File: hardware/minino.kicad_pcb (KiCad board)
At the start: 2 copper layers, 45 x 68 mm, 55 parts, among them J1 OLED, J2 GPS, J3 Battery, P1 USB_C_Plug_USB2.0, Q1 DMG3415U-7, Q2 PN2222A, SW1 ON, SW2 RIGHT, SW3 LEFT, SW4 DOWN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

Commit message: Replace_Labels
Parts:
- moved kibuzzard-6397A6E0 96.6 mm to (195.1, 91.4)
- moved kibuzzard-6398BE6D 92.2 mm to (200.9, 42.7), turned to 180 degrees
- moved kibuzzard-6397A7CD 89.3 mm to (186.8, 82.9)
- moved kibuzzard-6397A7DE 88.2 mm to (186.8, 98.4)
- moved kibuzzard-6397A7B6 84.2 mm to (186.7, 74.4)
- moved kibuzzard-6397B2CD 83.4 mm to (181.1, 98.6), turned to 0 degrees
- moved kibuzzard-6397A6F6 82.0 mm to (178.1, 91.4)
- moved kibuzzard-6398BE5A 78.5 mm to (172.7, 42.6), turned to 180 degrees
- moved kibuzzard-6397B2B5 71.4 mm to (175.5, 98.6), turned to 0 degrees
- moved kibuzzard-6398F328 3.70 mm to (195.2, 75.7)
- moved U3 1.15 mm to (195.2, 78.3)
- moved C6 1.03 mm to (195.5, 81.3)
- moved F1 0.89 mm to (204.0, 76.1)
- moved D1 0.35 mm to (194.7, 73.8)
- moved SW1 0.26 mm to (177.8, 94.7)
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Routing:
- net +3V3: track 93.5 -> 97.1 mm
- net /D-: track 31.7 -> 29.4 mm
- net /D+: track 31.4 -> 29.2 mm
- net Net-(C5-Pad1): track 35.8 -> 36.7 mm
- net Net-(F1-Pad1): track 15.3 -> 16.2 mm
- net /LED2: track 21.6 -> 22.3 mm

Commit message: Add_Logo
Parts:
- removed kibuzzard-6398BE5A: G***, kibuzzard-6398BE5A
- removed kibuzzard-6398BE6D: G***, kibuzzard-6398BE6D
- added G***: LOGO, Aesthetics:minino, F.Cu at (170.1, 80.4)
- added G***: LOGO, Aesthetics:minino, B.Cu at (185.6, 83.4)
- added G***: LOGO, Aesthetics:minino_simbolo, B.Cu at (185.9, 92.3)
- added kibuzzard-63BDBE6F: G***, kibuzzard-63BDBE6F, B.Cu at (172.9, 42.7)
- added kibuzzard-63BDBE87: G***, kibuzzard-63BDBE87, B.Cu at (200.4, 42.7)
- moved D1 21.8 mm to (197.0, 95.5)
- moved R4 21.7 mm to (193.3, 95.6)
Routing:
- net VBUS: track 55.8 -> 80.8 mm, vias 0 -> 2
- net Net-(R4-Pad1): track 6.98 -> 29.9 mm, vias 0 -> 2
- net GND: track 20.8 -> 21.6 mm
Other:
- board text added: "V1.0"
- board text removed: "Minino V1.0"

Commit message: update usb
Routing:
- net /D+: track 29.2 -> 26.6 mm

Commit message: Update_BOM
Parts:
- Q2: value PN2222A -> MMBT2222A
- moved Ref** 0.13 mm to (257.8, 152.5)
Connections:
- Q2 pad 1: GND -> (no net)
- Q2 pad 2: Net-(Q2-Pad2) -> GND
- R6 pad 2: Net-(Q2-Pad2) -> Net-(Q2-Pad1)
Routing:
- net Net-(Q2-Pad1): track 0.00 -> 6.88 mm
- net GND: track 21.6 -> 25.4 mm
- net Net-(Q2-Pad2): track 1.58 -> 0.00 mm
- net Net-(D2-Pad1): track 43.5 -> 42.7 mm

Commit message: Update_HTML
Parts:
- R3: value 4K7 -> 2K
- R7: footprint Resistor_SMD:R_0603_1608Metric_Pad0.98x0.95mm_HandSolder -> Resistor_SMD:R_0603_1608Metric
- moved Ref** 0.07 mm to (257.7, 152.4)
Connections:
- Q2 pad 1: (no net) -> Net-(Q2-Pad1)

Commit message: Add_example
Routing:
- net /D+: track 26.6 -> 31.7 mm
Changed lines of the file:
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@@
   (segment (start 198.585 76.82) (end 198.61 76.845) (width 0.3) (layer "B.Cu") (net 13))
   (segment (start 199.3925 82.16) (end 200.5675 82.16) (width 0.3) (layer "B.Cu") (net 13))
-  (segment (start 197.903986 64.840486) (end 198.706873 64.037599) (width 0.1524) (layer "F.Cu") (net 14))
-  (segment (start 197.903986 83.236014) (end 197.903986 64.840486) (width 0.1524) (layer "F.Cu") (net 14))
-  (segment (start 199.356201 64.037599) (end 199.58 63.8138) (width 0.1524) (layer "F.Cu") (net 14))
-  (segment (start 198.706873 64.037599) (end 199.356201 64.037599) (width 0.1524) (layer "F.Cu") (net 14))
+  (segment (start 198.930672 63.8138) (end 197.903986 64.840486) (width 0.1524) (layer "F.Cu") (net 14))
+  (segment (start 197.903986 83.062879) (end 198.473007 83.6319) (width 0.1524) (layer "F.Cu") (net 14))
+  (segment (start 199.58 63.8138) (end 198.930672 63.8138) (width 0.1524) (layer "F.Cu") (net 14))
+  (segment (start 197.903986 64.840486) (end 197.903986 83.062879) (width 0.1524) (layer "F.Cu") (net 14))
   (via (at 199.58 63.8138) (size 0.6) (drill 0.3) (layers "F.Cu" "B.Cu") (net 14))
-  (via (at 197.903986 83.236014) (size 0.6) (drill 0.3) (layers "F.Cu" "B.Cu") (net 14))
+  (via (at 198.473007 83.6319) (size 0.6) (drill 0.3) (layers "F.Cu" "B.Cu") (net 14))
   (segment (start 198.137601 63.6676) (end 197.655001 63.185) (width 0.1524) (layer "B.Cu") (net 14))
-  (segment (start 198.546873 83.5624) (end 198.220487 83.236014) (width 0.1524) (layer "B.Cu") (net 14))
-  (segment (start 199.232399 83.5624) (end 198.546873 83.5624) (width 0.1524) (layer "B.Cu") (net 14))
-  (segment (start 199.329999 83.66) (end 199.232399 83.5624) (width 0.1524) (layer "B.Cu") (net 14))
   (segment (start 201.85 83.3549) (end 201.85 82.9651) (width 0.1524) (layer "B.Cu") (net 14))
+  (segment (start 200.5675 83.66) (end 198.501107 83.66) (width 0.1524) (layer "B.Cu") (net 14))
+  (segment (start 198.501107 83.66) (end 198.473007 83.6319) (width 0.1524) (layer "B.Cu") (net 14))
   (segment (start 201.5449 82.66) (end 200.5675 82.66) (width 0.1524) (layer "B.Cu") (net 14))
   (segment (start 199.112453 63.6676) (end 198.137601 63.6676) (width 0.1524) (layer "B.Cu") (net 14))
@@
   (segment (start 201.85 82.9651) (end 201.5449 82.66) (width 0.1524) (layer "B.Cu") (net 14))
   (segment (start 200.5675 83.66) (end 201.5449 83.66) (width 0.1524) (layer "B.Cu") (net 14))
-  (segment (start 200.5675 83.66) (end 199.329999 83.66) (width 0.1524) (layer "B.Cu") (net 14))
   (segment (start 199.58 63.8138) (end 199.258653 63.8138) (width 0.1524) (layer "B.Cu") (net 14))
   (segment (start 201.5449 83.66) (end 201.85 83.3549) (width 0.1524) (layer "B.Cu") (net 14))
   (segment (start 197.655001 63.185) (end 196.53 63.185) (width 0.1524) (layer "B.Cu") (net 14))
-  (segment (start 198.220487 83.236014) (end 197.903986 83.236014) (width 0.1524) (layer "B.Cu") (net 14))
   (segment (start 198.833127 64.342401) (end 198.208786 64.966742) (width 0.1524) (layer "F.Cu") (net 15))
   (segment (start 198.208786 66.818786) (end 198.208786 66.868786) (width 0.1524) (layer "F.Cu") (net 15))
@@
   (arc (start 198.508786 66.518786) (mid 198.296654 66.606654) (end 198.208786 66.818786) (width 0.1524) (layer "F.Cu") (net 15))
   (arc (start 198.6713 65.918786) (mid 198.883432 66.006654) (end 198.9713 66.218786) (width 0.1524) (layer "F.Cu") (net 15))
+  (segment (start 197.35 83.61) (end 197.35 83.14) (width 0.1524) (layer "B.Cu") (net 15))
   (segment (start 197.655001 64.455) (end 196.53 64.455) (width 0.1524) (layer "B.Cu") (net 15))
-  (segment (start 199.232399 83.2576) (end 198.673127 83.2576) (width 0.1524) (layer "B.Cu") (net 15))
-  (segment (start 198.673127 83.2576) (end 198.436014 83.020487) (width 0.1524) (layer "B.Cu") (net 15))
-  (segment (start 199.329999 83.16) (end 199.232399 83.2576) (width 0.1524) (layer "B.Cu") (net 15))
-  (segment (start 200.5675 83.16) (end 199.329999 83.16) (width 0.1524) (layer "B.Cu") (net 15))
+  (segment (start 200.5675 83.16) (end 198.747264 83.16) (width 0.1524) (layer "B.Cu") (net 15))
+  (segment (start 198.691754 83.10449) (end 198.520017 83.10449) (width 0.1524) (layer "B.Cu") (net 15))
+  (segment (start 198.747264 83.16) (end 198.691754 83.10449) (width 0.1524) (layer "B.Cu") (net 15))
+  (segment (start 200.5675 84.16) (end 197.9 84.16) (width 0.1524) (layer "B.Cu") (net 15))
+  (segment (start 197.786014 82.703986) (end 198.436014 82.703986) (width 0.1524) (layer "B.Cu") (net 15))
+  (segment (start 197.35 83.14) (end 197.786014 82.703986) (width 0.1524) (layer "B.Cu") (net 15))
   (segment (start 198.9862 63.9724) (end 198.137601 63.9724) (width 0.1524) (layer "B.Cu") (net 15))
   (segment (start 199.58 64.5662) (end 198.9862 63.9724) (width 0.1524) (layer "B.Cu") (net 15))
   (segment (start 198.137601 63.9724) (end 197.655001 64.455) (width 0.1524) (layer "B.Cu") (net 15))
+  (segment (start 198.520017 83.10449) (end 198.436014 83.020487) (width 0.1524) (layer "B.Cu") (net 15))
   (segment (start 198.436014 83.020487) (end 198.436014 82.703986) (width 0.1524) (layer "B.Cu") (net 15))
+  (segment (start 197.9 84.16) (end 197.35 83.61) (width 0.1524) (layer "B.Cu") (net 15))
   (segment (start 199.3925 85.16) (end 198.9025 85.65) (width 0.3) (layer "B.Cu") (net 16))
   (segment (start 198.9025 85.65) (end 198.075 85.65) (width 0.3) (layer "B.Cu") (net 16))

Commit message: Add_example_spoof
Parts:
- moved kibuzzard-6398F328 18.1 mm to (196.5, 93.7)
- moved kibuzzard-6397B2B5 5.77 mm to (181.3, 98.8)
- moved kibuzzard-6397B2CD 4.99 mm to (176.2, 98.7)
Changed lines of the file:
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@@
   )
   (footprint "kibuzzard-6397B2CD" (layer "F.Cu")
-    (at 181.14 98.552)
+    (at 176.15 98.67)
     (descr "Converted using: scripting")
     (tags "svg2mod")
@@
   )
   (footprint "kibuzzard-6397B2B5" (layer "F.Cu")
-    (at 175.514 98.552)
+    (at 181.28 98.76)
     (descr "Converted using: scripting")
     (tags "svg2mod")
@@
   )
   (footprint "kibuzzard-6398F328" (layer "B.Cu")
-    (at 195.25 75.72 180)
+    (at 196.52 93.74 180)
     (descr "Converted using: scripting")
     (tags "svg2mod")
@@
   (segment (start 198.585 76.82) (end 198.61 76.845) (width 0.3) (layer "B.Cu") (net 13))
   (segment (start 199.3925 82.16) (end 200.5675 82.16) (width 0.3) (layer "B.Cu") (net 13))
-  (segment (start 198.930672 63.8138) (end 197.903986 64.840486) (width 0.1524) (layer "F.Cu") (net 14))
-  (segment (start 197.903986 83.062879) (end 198.473007 83.6319) (width 0.1524) (layer "F.Cu") (net 14))
+  (segment (start 197.58 65.164472) (end 197.58 82.68) (width 0.1524) (layer "F.Cu") (net 14))
   (segment (start 199.58 63.8138) (end 198.930672 63.8138) (width 0.1524) (layer "F.Cu") (net 14))
-  (segment (start 197.903986 64.840486) (end 197.903986 83.062879) (width 0.1524) (layer "F.Cu") (net 14))
+  (segment (start 198.930672 63.8138) (end 197.58 65.164472) (width 0.1524) (layer "F.Cu") (net 14))
   (via (at 199.58 63.8138) (size 0.6) (drill 0.3) (layers "F.Cu" "B.Cu") (net 14))
-  (via (at 198.473007 83.6319) (size 0.6) (drill 0.3) (layers "F.Cu" "B.Cu") (net 14))
+  (via (at 197.58 82.68) (size 0.6) (drill 0.3) (layers "F.Cu" "B.Cu") (net 14))
+  (segment (start 198.73 83.16) (end 198.79 83.16) (width 0.1524) (layer "B.Cu") (net 14))
+  (segment (start 198.83 83.16) (end 198.96 83.29) (width 0.1524) (layer "B.Cu") (net 14))
+  (segment (start 199.33 83.66) (end 198.96 83.29) (width 0.1524) (layer "B.Cu") (net 14))
+  (segment (start 200.5675 83.66) (end 199.33 83.66) (width 0.1524) (layer "B.Cu") (net 14))
+  (segment (start 198.79 83.16) (end 198.96 82.99) (width 0.1524) (layer "B.Cu") (net 14))
   (segment (start 198.137601 63.6676) (end 197.655001 63.185) (width 0.1524) (layer "B.Cu") (net 14))
-  (segment (start 201.85 83.3549) (end 201.85 82.9651) (width 0.1524) (layer "B.Cu") (net 14))
-  (segment (start 200.5675 83.66) (end 198.501107 83.66) (width 0.1524) (layer "B.Cu") (net 14))
-  (segment (start 198.501107 83.66) (end 198.473007 83.6319) (width 0.1524) (layer "B.Cu") (net 14))
-  (segment (start 201.5449 82.66) (end 200.5675 82.66) (width 0.1524) (layer "B.Cu") (net 14))
+  (segment (start 198.96 83.16) (end 198.73 83.16) (width 0.1524) (layer "B.Cu") (net 14))
+  (segment (start 199.29 82.66) (end 200.5675 82.66) (width 0.1524) (layer "B.Cu") (net 14))
+  (segment (start 198.06 83.16) (end 197.58 82.68) (width 0.1524) (layer "B.Cu") (net 14))
   (segment (start 199.112453 63.6676) (end 198.137601 63.6676) (width 0.1524) (layer "B.Cu") (net 14))
+  (segment (start 198.79 83.16) (end 198.83 83.16) (width 0.1524) (layer "B.Cu") (net 14))
   (segment (start 199.258653 63.8138) (end 199.112453 63.6676) (width 0.1524) (layer "B.Cu") (net 14))
-  (segment (start 201.85 82.9651) (end 201.5449 82.66) (width 0.1524) (layer "B.Cu") (net 14))
-  (segment (start 200.5675 83.66) (end 201.5449 83.66) (width 0.1524) (layer "B.Cu") (net 14))
+  (segment (start 198.96 83.29) (end 198.96 83.16) (width 0.1524) (layer "B.Cu") (net 14))
+  (segment (start 198.73 83.16) (end 198.06 83.16) (width 0.1524) (layer "B.Cu") (net 14))
+  (segment (start 198.96 83.16) (end 198.96 82.99) (width 0.1524) (layer "B.Cu") (net 14))
   (segment (start 199.58 63.8138) (end 199.258653 63.8138) (width 0.1524) (layer "B.Cu") (net 14))
-  (segment (start 201.5449 83.66) (end 201.85 83.3549) (width 0.1524) (layer "B.Cu") (net 14))
   (segment (start 197.655001 63.185) (end 196.53 63.185) (width 0.1524) (layer "B.Cu") (net 14))
-  (segment (start 198.833127 64.342401) (end 198.208786 64.966742) (width 0.1524) (layer "F.Cu") (net 15))
-  (segment (start 198.208786 66.818786) (end 198.208786 66.868786) (width 0.1524) (layer "F.Cu") (net 15))
-  (segment (start 198.208786 82.476758) (end 198.436014 82.703986) (width 0.1524) (layer "F.Cu") (net 15))
-  (segment (start 199.356201 64.342401) (end 198.833127 64.342401) (width 0.1524) (layer "F.Cu") (net 15))
-  (segment (start 198.208786 66.868786) (end 198.208786 82.476758) (width 0.1524) (layer "F.Cu") (net 15))
-  (segment (start 198.208786 64.966742) (end 198.208786 65.618786) (width 0.1524) (layer "F.Cu") (net 15))
+  (segment (start 198.96 82.99) (end 199.29 82.66) (width 0.1524) (layer "B.Cu") (net 14))
   (segment (start 199.58 64.5662) (end 199.356201 64.342401) (width 0.1524) (layer "F.Cu") (net 15))
-  (segment (start 198.6713 66.518786) (end 198.508786 66.518786) (width 0.1524) (layer "F.Cu") (net 15))
+  (segment (start 198.208786 83.211214) (end 197.69 83.73) (width 0.1524) (layer "F.Cu") (net 15))
+  (segment (start 198.208786 64.966742) (end 198.208786 65.618786) (width 0.1524) (layer "F.Cu") (net 15))
+  (segment (start 198.208786 82.476758) (end 198.208786 83.211214) (width 0.1524) (layer "F.Cu") (net 15))
   (segment (start 198.508786 65.918786) (end 198.6713 65.918786) (width 0.1524) (layer "F.Cu") (net 15))
-  (via (at 198.436014 82.703986) (size 0.6) (drill 0.3) (layers "F.Cu" "B.Cu") (net 15))
+  (segment (start 198.833127 64.342401) (end 198.208786 64.966742) (width 0.1524) (layer "F.Cu") (net 15))
+  (segment (start 198.6713 66.518786) (end 198.508786 66.518786) (width 0.1524) (layer "F.Cu") (net 15))
+  (segment (start 199.356201 64.342401) (end 198.833127 64.342401) (width 0.1524) (layer "F.Cu") (net 15))
+  (segment (start 198.208786 66.818786) (end 198.208786 82.476758) (width 0.1524) (layer "F.Cu") (net 15))
+  (via (at 197.69 83.73) (size 0.6) (drill 0.3) (layers "F.Cu" "B.Cu") (net 15))
   (via (at 199.58 64.5662) (size 0.6) (drill 0.3) (layers "F.Cu" "B.Cu") (net 15))
-  (arc (start 198.9713 66.218786) (mid 198.883432 66.430918) (end 198.6713 66.518786) (width 0.1524) (layer "F.Cu") (net 15))
-  (arc (start 198.208786 65.618786) (mid 198.296654 65.830918) (end 198.508786 65.918786) (width 0.1524) (layer "F.Cu") (net 15))
-  (arc (start 198.508786 66.518786) (mid 198.296654 66.606654) (end 198.208786 66.818786) (width 0.1524) (layer "F.Cu") (net 15))
   (arc (start 198.6713 65.918786) (mid 198.883432 66.006654) (end 198.9713 66.218786) (width 0.1524) (layer "F.Cu") (net 15))
-  (segment (start 197.35 83.61) (end 197.35 83.14) (width 0.1524) (layer "B.Cu") (net 15))
+  (arc (start 198.508786 66.518786) (mid 198.296654 66.606654) (end 198.208786 66.818786) (width 0.1524) (layer "F.Cu") (net 15))
+  (arc (start 198.208786 65.618786) (mid 198.296654 65.830918) (end 198.508786 65.918786) (width 0.1524) (layer "F.Cu") (net 15))
+  (arc (start 198.9713 66.218786) (mid 198.883432 66.430918) (end 198.6713 66.518786) (width 0.1524) (layer "F.Cu") (net 15))
+  (segment (start 201.5449 84.16) (end 200.5675 84.16) (width 0.1524) (layer "B.Cu") (net 15))
   (segment (start 197.655001 64.455) (end 196.53 64.455) (width 0.1524) (layer "B.Cu") (net 15))
-  (segment (start 200.5675 83.16) (end 198.747264 83.16) (width 0.1524) (layer "B.Cu") (net 15))
-  (segment (start 198.691754 83.10449) (end 198.520017 83.10449) (width 0.1524) (layer "B.Cu") (net 15))
-  (segment (start 198.747264 83.16) (end 198.691754 83.10449) (width 0.1524) (layer "B.Cu") (net 15))
-  (segment (start 200.5675 84.16) (end 197.9 84.16) (width 0.1524) (layer "B.Cu") (net 15))
-  (segment (start 197.786014 82.703986) (end 198.436014 82.703986) (width 0.1524) (layer "B.Cu") (net 15))
-  (segment (start 197.35 83.14) (end 197.786014 82.703986) (width 0.1524) (layer "B.Cu") (net 15))
+  (segment (start 201.5449 83.16) (end 201.6211 83.2362) (width 0.1524) (layer "B.Cu") (net 15))
+  (segment (start 200.5675 84.16) (end 198.12 84.16) (width 0.1524) (layer "B.Cu") (net 15))
+  (segment (start 200.5675 83.16) (end 201.5449 83.16) (width 0.1524) (layer "B.Cu") (net 15))
+  (segment (start 201.6211 84.0838) (end 201.5449 84.16) (width 0.1524) (layer "B.Cu") (net 15))
   (segment (start 198.9862 63.9724) (end 198.137601 63.9724) (width 0.1524) (layer "B.Cu") (net 15))
   (segment (start 199.58 64.5662) (end 198.9862 63.9724) (width 0.1524) (layer "B.Cu") (net 15))
   (segment (start 198.137601 63.9724) (end 197.655001 64.455) (width 0.1524) (layer "B.Cu") (net 15))
-  (segment (start 198.520017 83.10449) (end 198.436014 83.020487) (width 0.1524) (layer "B.Cu") (net 15))
-  (segment (start 198.436014 83.020487) (end 198.436014 82.703986) (width 0.1524) (layer "B.Cu") (net 15))
-  (segment (start 197.9 84.16) (end 197.35 83.61) (width 0.1524) (layer "B.Cu") (net 15))
+  (segment (start 198.12 84.16) (end 197.69 83.73) (width 0.1524) (layer "B.Cu") (net 15))
+  (segment (start 201.6211 83.2362) (end 201.6211 84.0838) (width 0.1524) (layer "B.Cu") (net 15))
   (segment (start 199.3925 85.16) (end 198.9025 85.65) (width 0.3) (layer "B.Cu") (net 16))
   (segment (start 198.9025 85.65) (end 198.075 85.65) (width 0.3) (layer "B.Cu") (net 16))

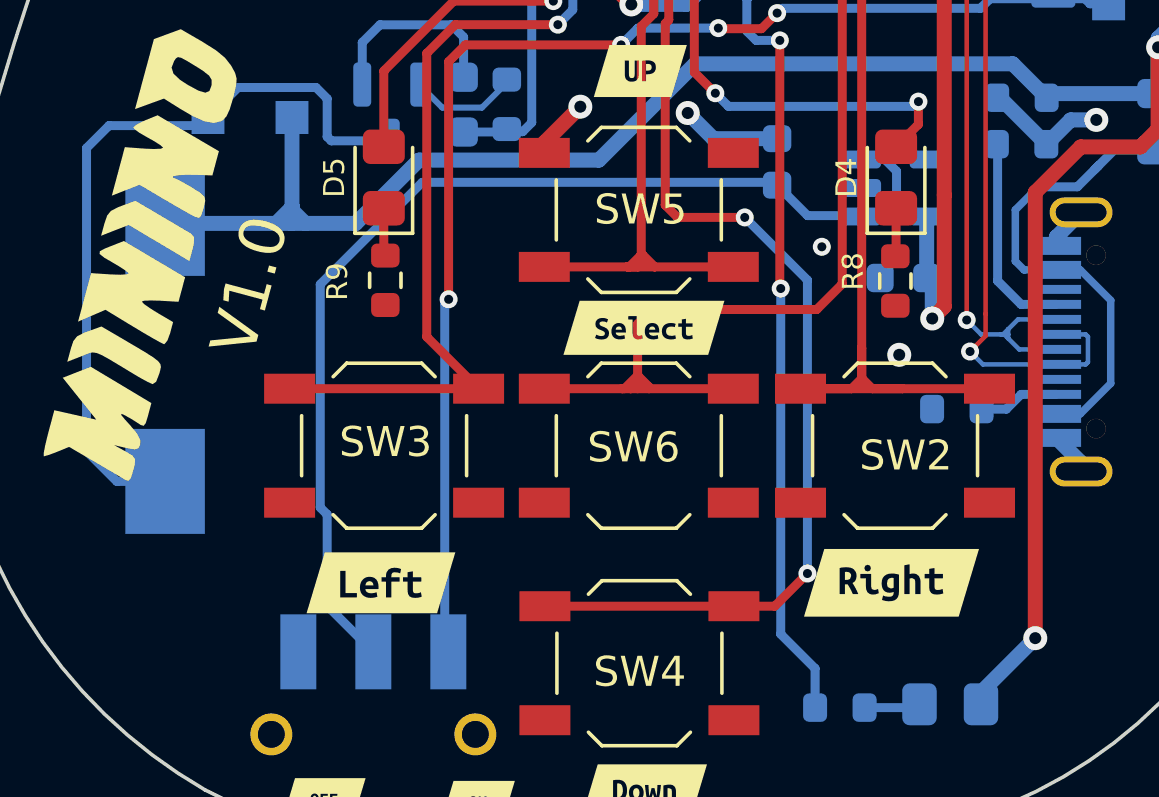
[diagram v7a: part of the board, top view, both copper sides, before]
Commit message: Change_Labels
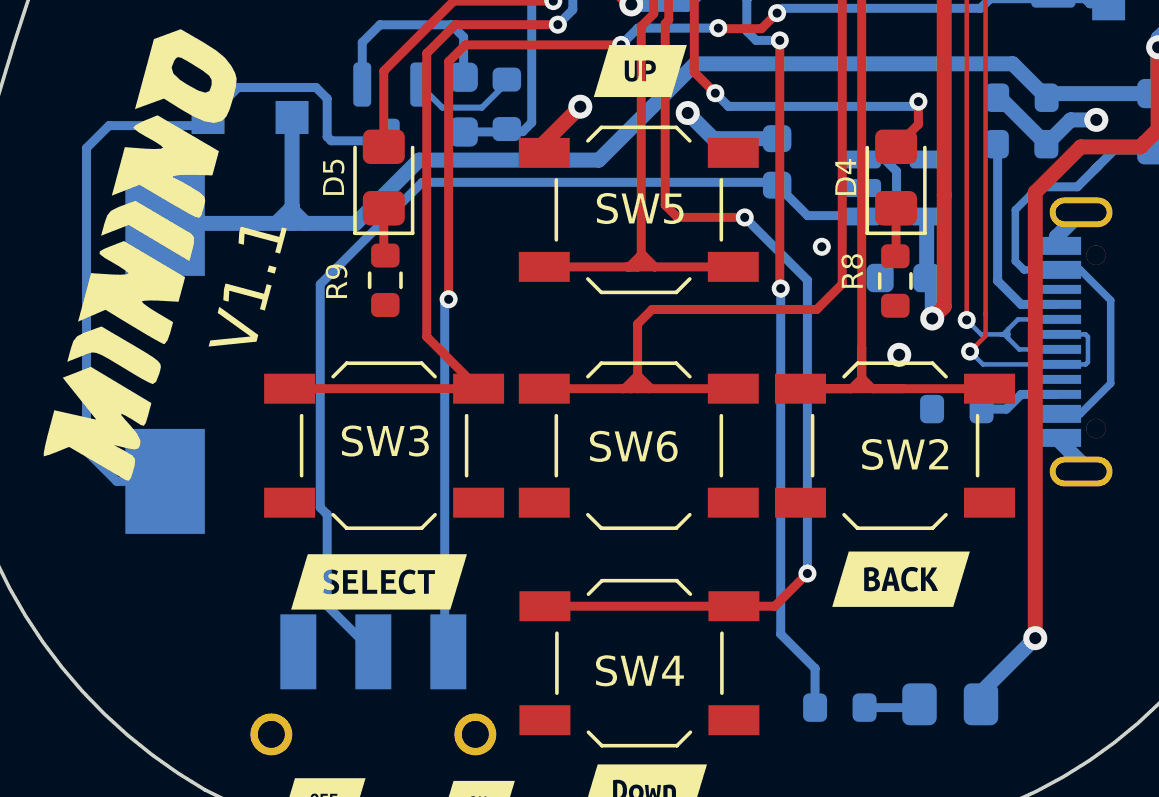
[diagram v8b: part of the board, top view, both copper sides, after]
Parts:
- removed kibuzzard-6397A6E0: G***, kibuzzard-6397A6E0
- removed kibuzzard-6397A6F6: G***, kibuzzard-6397A6F6
- removed kibuzzard-6397A7CD: G***, kibuzzard-6397A7CD
- added kibuzzard-640900FA: G***, kibuzzard-640900FA, F.Cu at (195.4, 91.3)
- added kibuzzard-6409010E: G***, kibuzzard-6409010E, F.Cu at (178.0, 91.4)
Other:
- board text added: "V1.1"
